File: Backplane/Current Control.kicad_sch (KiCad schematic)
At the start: 28 parts, among them Q1 TPHR8504PL,LQ(M1W, Q2 TPHR8504PL,LQ(M1W, U1 LM393, U10 LM393, U11 LM358, U14 MCP4725A0T-E/CH, U2 LM358, U7 UCC27324DR, U9 MCP4725A0T-E/CH

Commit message: Almost done with components.
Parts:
- added R13, R14: 1k, Resistor_SMD:R_1206_3216Metric_Pad1.30x1.75mm_HandSolder, symbol Device:R
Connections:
- net at R2.2, R5.1, U11.1: now also R14.2
- net at R10.1, R8.2, U2.7: now also R13.2
- new net LOAD_A_SNS: R13.1
- new net LOAD_B_SNS: R14.1

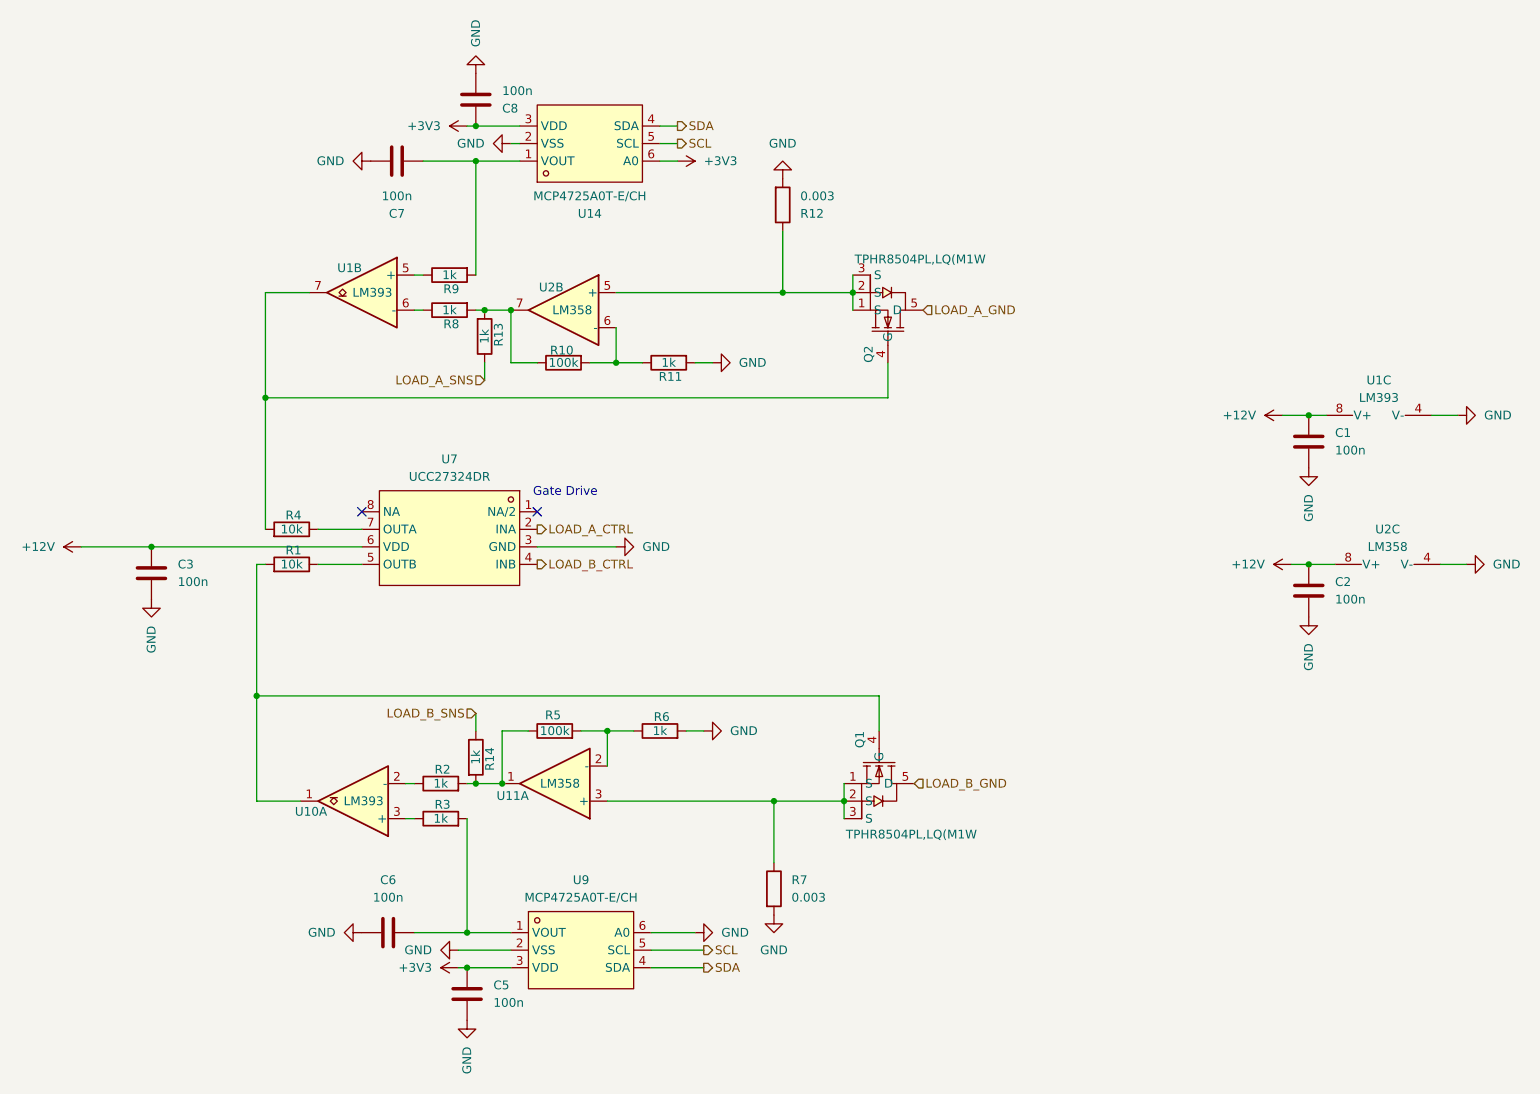
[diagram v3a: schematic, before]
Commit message: Working on splitting up I2C
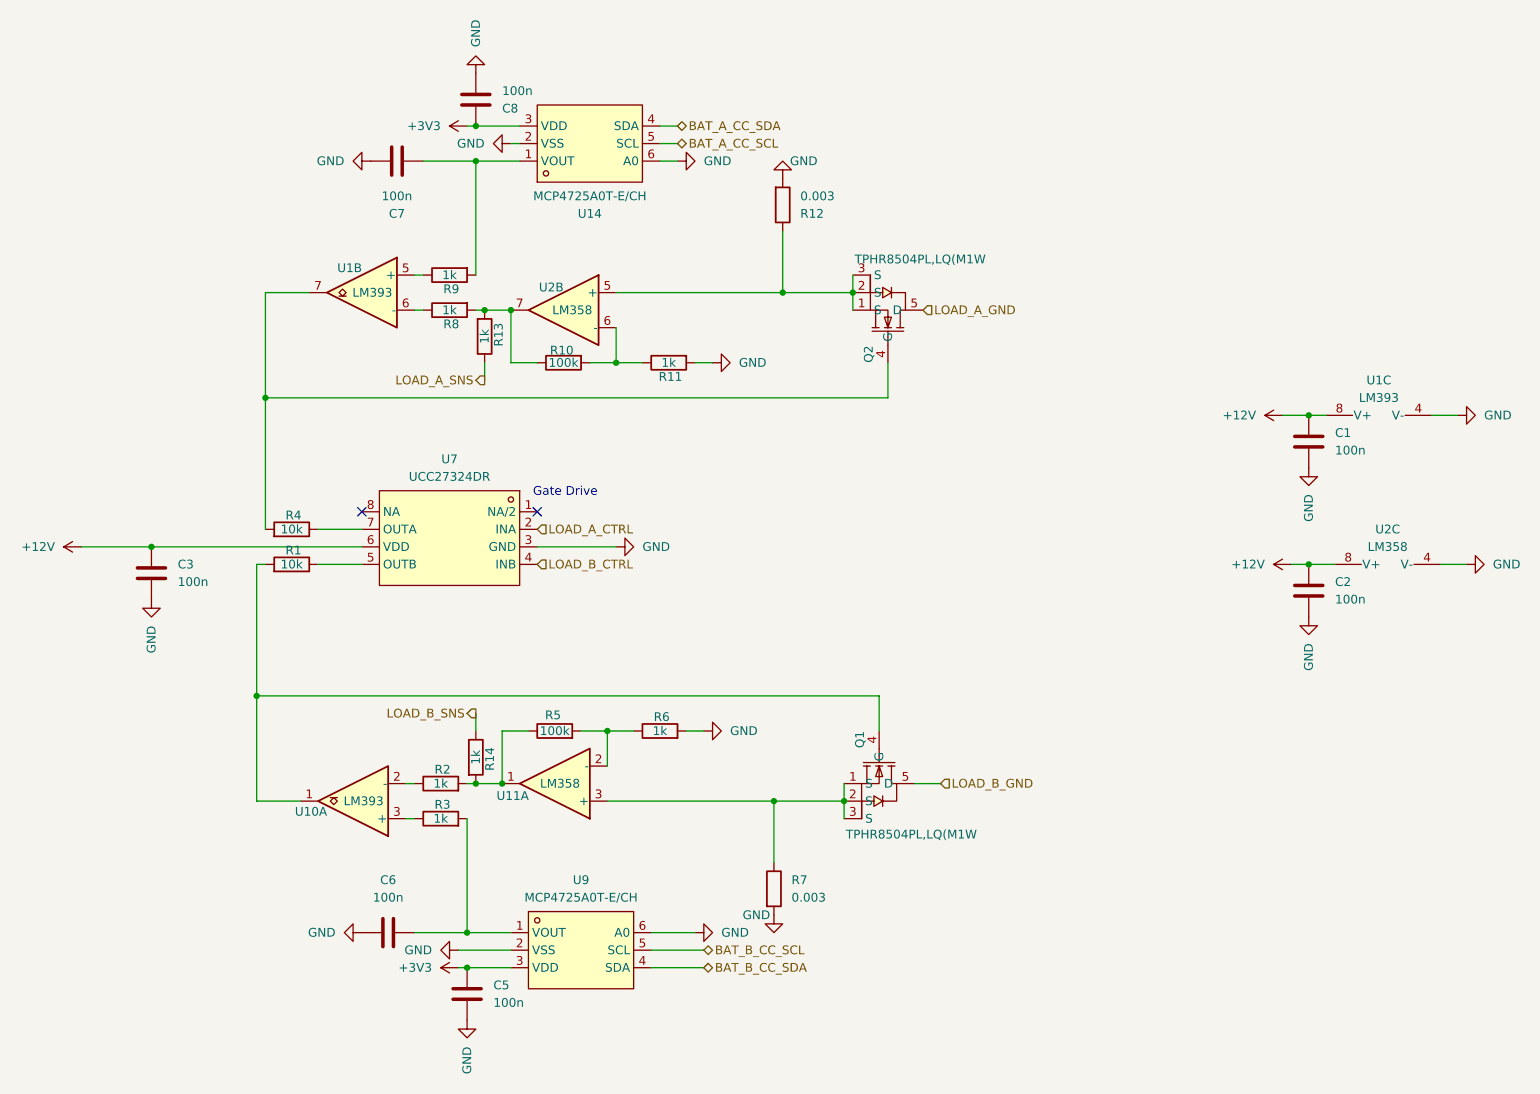
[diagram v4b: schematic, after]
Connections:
- net +3V3: no longer U14.6 (A0)
- net GND: now also U14.6 (A0)
- net SCL renamed BAT_A_CC_SCL
- net BAT_A_CC_SCL: no longer U9.5 (SCL)
- net SDA renamed BAT_A_CC_SDA
- net BAT_A_CC_SDA: no longer U9.4 (SDA)
- new net BAT_B_CC_SCL: U9.5 (SCL)
- new net BAT_B_CC_SDA: U9.4 (SDA)
